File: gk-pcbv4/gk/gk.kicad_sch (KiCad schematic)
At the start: 4 parts

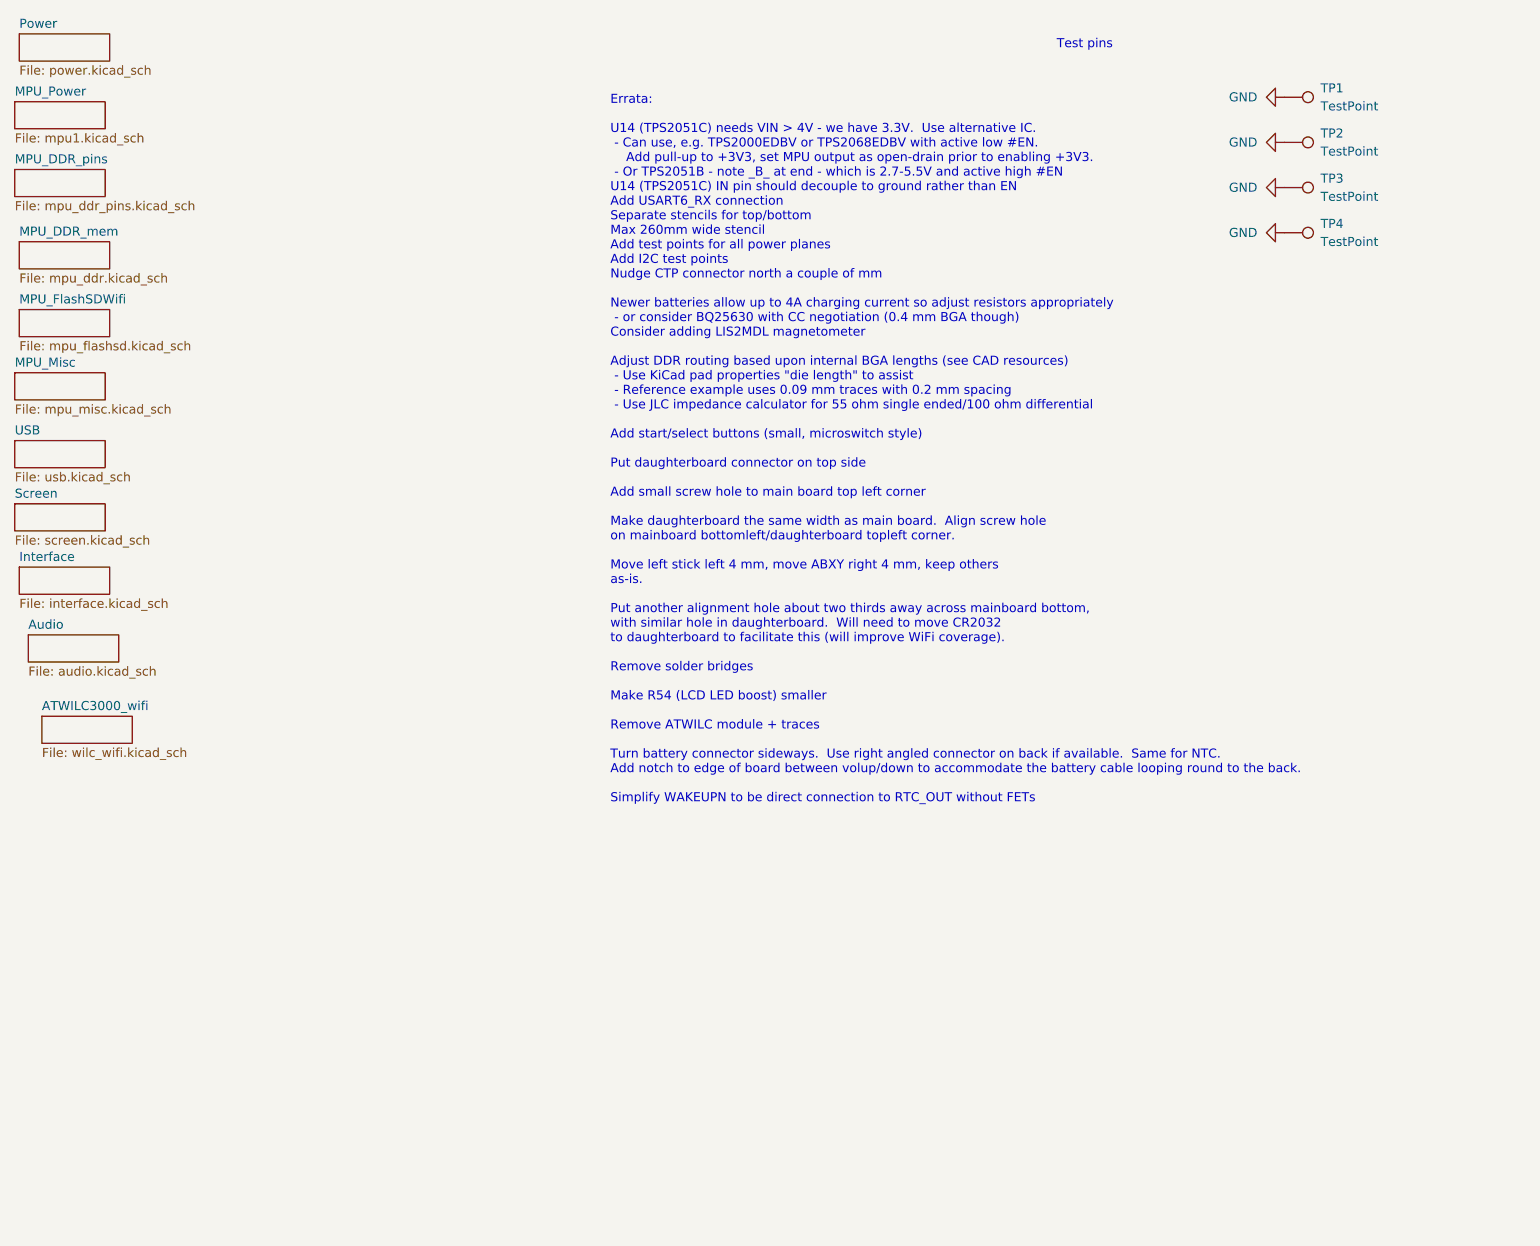
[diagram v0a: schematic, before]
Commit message: add v2 controls board
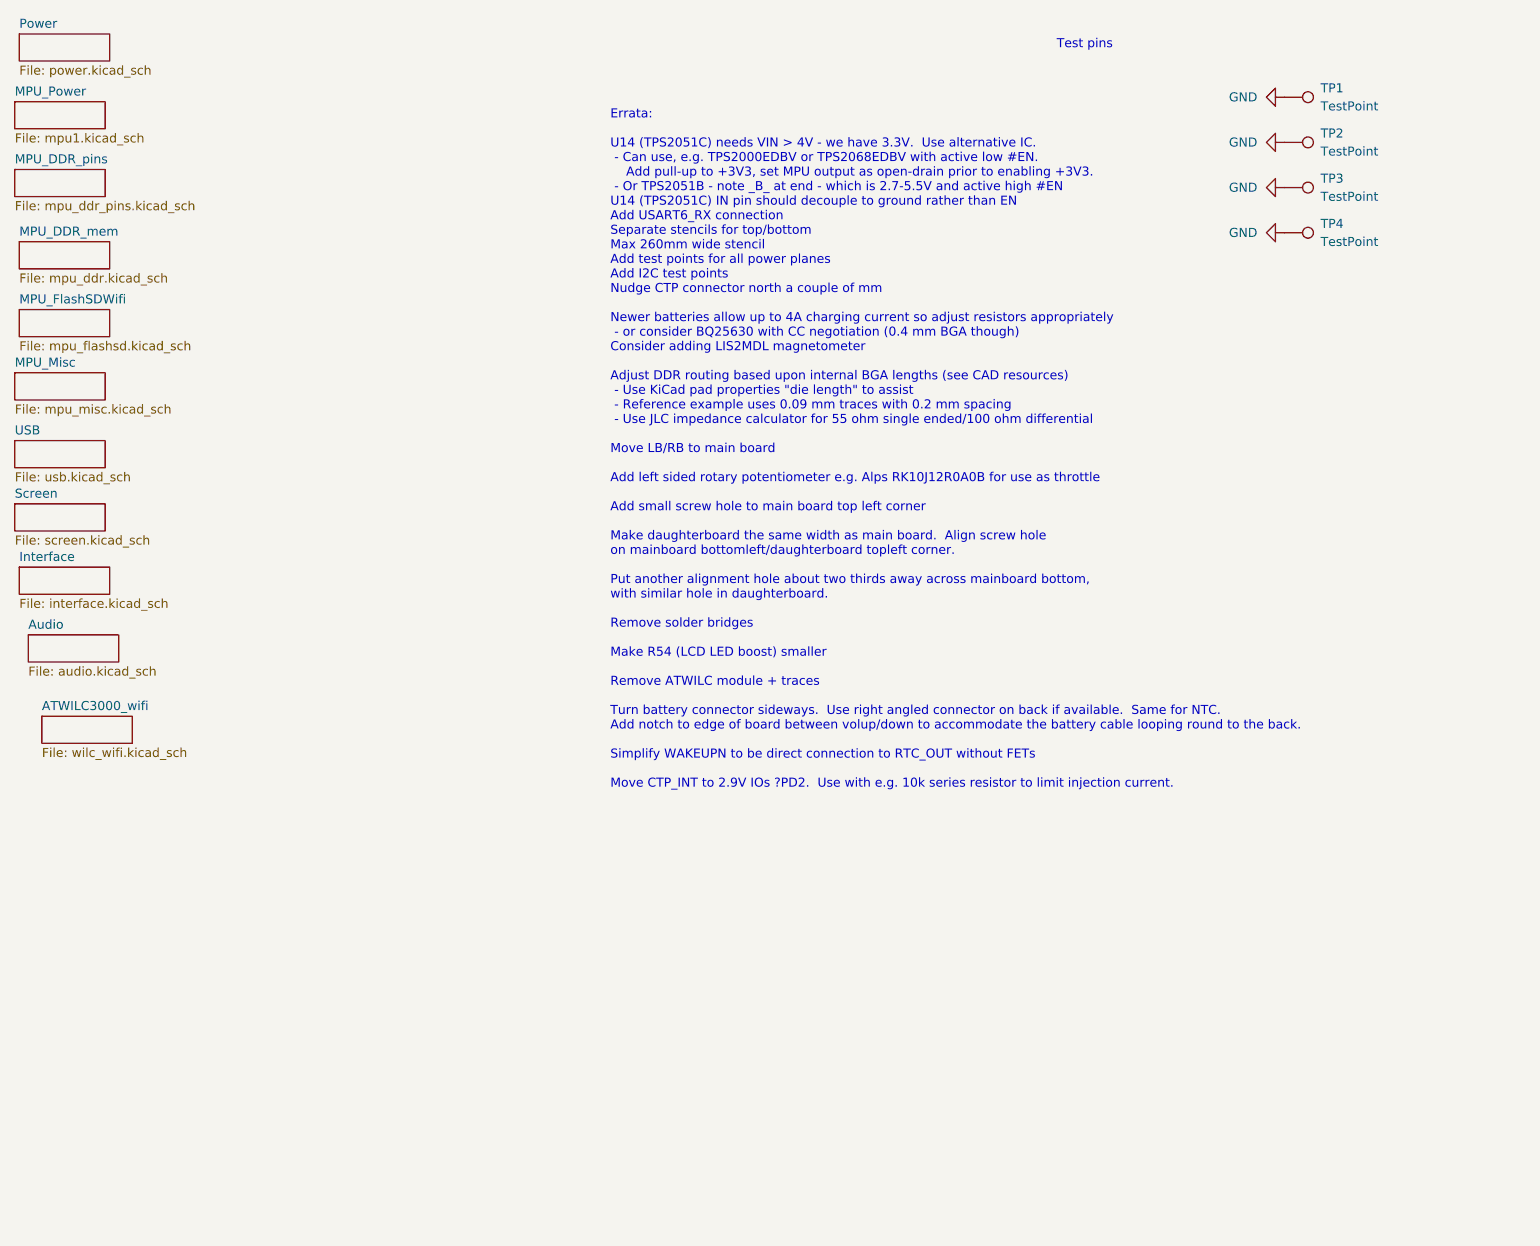
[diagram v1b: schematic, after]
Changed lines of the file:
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@@
 		)
 	)
-	(text "Errata:\n\nU14 (TPS2051C) needs VIN > 4V - we have 3.3V.  Use alternative IC.\n - Can use, e.g. TPS2000EDBV or TPS2068EDBV with active low #EN.\n    Add pull-up to +3V3, set MPU output as open-drain prior to enabling +3V3.\n - Or TPS2051B - note _B_ at end - which is 2.7-5.5V and active high #EN\nU14 (TPS2051C) IN pin should decouple to ground rather than EN\nAdd USART6_RX connection\nSeparate stencils for top/bottom\nMax 260mm wide stencil\nAdd test points for all power planes\nAdd I2C test points\nNudge CTP connector north a couple of mm\n\nNewer batteries allow up to 4A charging current so adjust resistors appropriately\n - or consider BQ25630 with CC negotiation (0.4 mm BGA though)\nConsider adding LIS2MDL magnetometer\n\nAdjust DDR routing based upon internal BGA lengths (see CAD resources)\n - Use KiCad pad properties \"die length\" to assist\n - Reference example uses 0.09 mm traces with 0.2 mm spacing\n - Use JLC impedance calculator for 55 ohm single ended/100 ohm differential\n\nAdd start/select buttons (small, microswitch style)\n\nPut daughterboard connector on top side\n\nAdd small screw hole to main board top left corner\n\nMake daughterboard the same width as main board.  Align screw hole\non mainboard bottomleft/daughterboard topleft corner.\n\nMove left stick left 4 mm, move ABXY right 4 mm, keep others\nas-is.\n\nPut another alignment hole about two thirds away across mainboard bottom,\nwith similar hole in daughterboard.  Will need to move CR2032\nto daughterboard to facilitate this (will improve WiFi coverage).\n\nRemove solder bridges\n\nMake R54 (LCD LED boost) smaller\n\nRemove ATWILC module + traces\n\nTurn battery connector sideways.  Use right angled connector on back if available.  Same for NTC.\nAdd notch to edge of board between volup/down to accommodate the battery cable looping round to the back.\n\nSimplify WAKEUPN to be direct connection to RTC_OUT without FETs"
+	(text "Errata:\n\nU14 (TPS2051C) needs VIN > 4V - we have 3.3V.  Use alternative IC.\n - Can use, e.g. TPS2000EDBV or TPS2068EDBV with active low #EN.\n    Add pull-up to +3V3, set MPU output as open-drain prior to enabling +3V3.\n - Or TPS2051B - note _B_ at end - which is 2.7-5.5V and active high #EN\nU14 (TPS2051C) IN pin should decouple to ground rather than EN\nAdd USART6_RX connection\nSeparate stencils for top/bottom\nMax 260mm wide stencil\nAdd test points for all power planes\nAdd I2C test points\nNudge CTP connector north a couple of mm\n\nNewer batteries allow up to 4A charging current so adjust resistors appropriately\n - or consider BQ25630 with CC negotiation (0.4 mm BGA though)\nConsider adding LIS2MDL magnetometer\n\nAdjust DDR routing based upon internal BGA lengths (see CAD resources)\n - Use KiCad pad properties \"die length\" to assist\n - Reference example uses 0.09 mm traces with 0.2 mm spacing\n - Use JLC impedance calculator for 55 ohm single ended/100 ohm differential\n\nMove LB/RB to main board\n\nAdd left sided rotary potentiometer e.g. Alps RK10J12R0A0B for use as throttle\n\nAdd small screw hole to main board top left corner\n\nMake daughterboard the same width as main board.  Align screw hole\non mainboard bottomleft/daughterboard topleft corner.\n\nPut another alignment hole about two thirds away across mainboard bottom,\nwith similar hole in daughterboard.\n\nRemove solder bridges\n\nMake R54 (LCD LED boost) smaller\n\nRemove ATWILC module + traces\n\nTurn battery connector sideways.  Use right angled connector on back if available.  Same for NTC.\nAdd notch to edge of board between volup/down to accommodate the battery cable looping round to the back.\n\nSimplify WAKEUPN to be direct connection to RTC_OUT without FETs\n\nMove CTP_INT to 2.9V IOs ?PD2.  Use with e.g. 10k series resistor to limit injection current."
 		(exclude_from_sim no)
 		(at 104.648 80.01 0)

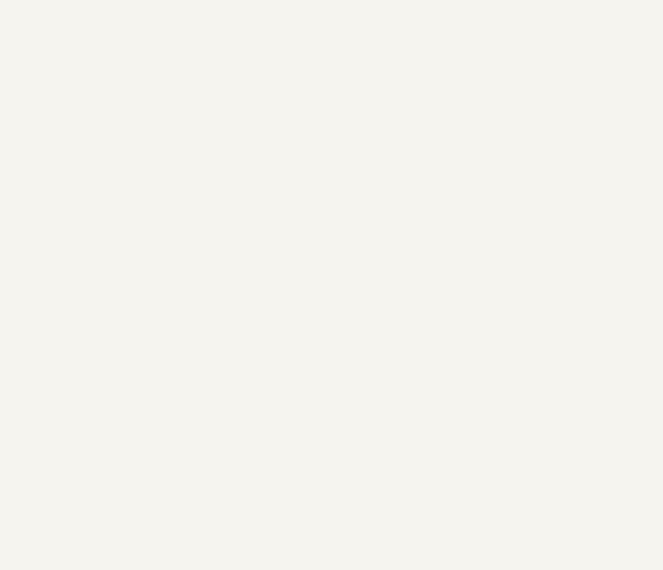
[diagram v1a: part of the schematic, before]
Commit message: update drill holes
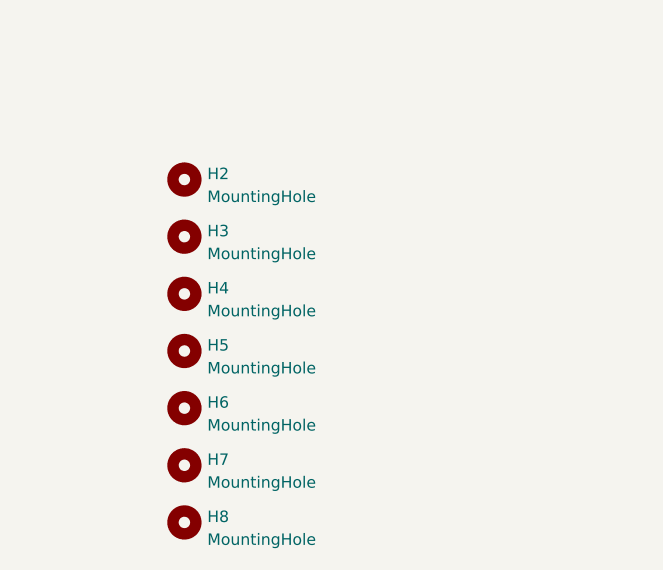
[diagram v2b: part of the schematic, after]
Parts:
- added H2, H3, H4, H5, H6, H7, H8: MountingHole, MountingHole:MountingHole_3.2mm_M3, symbol Mechanical:MountingHole
